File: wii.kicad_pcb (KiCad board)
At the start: 2 copper layers, 60.8 x 24 mm, 12 parts, among them J1 12401598E4#2A, J2 54102-0164, U2 AZ1117-3.3

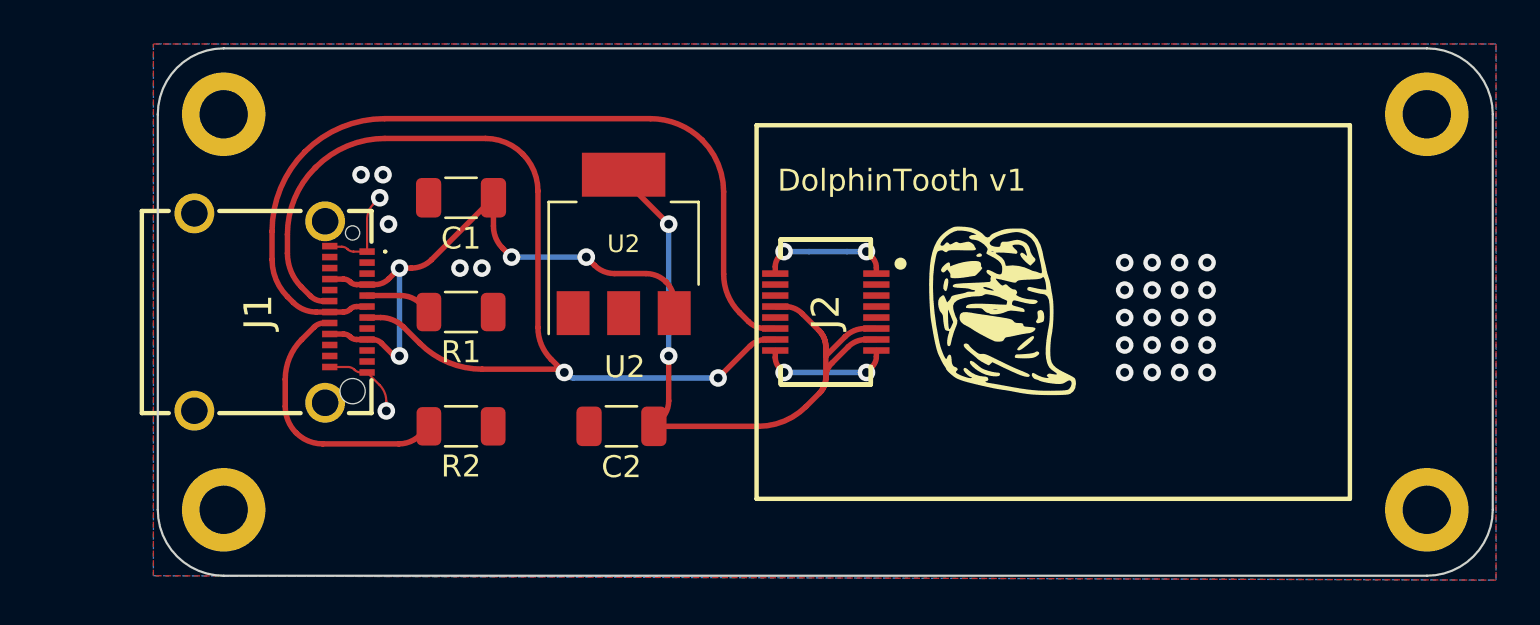
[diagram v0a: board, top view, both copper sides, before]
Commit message: change to usb b
also added html bom plugin and removed round tracks
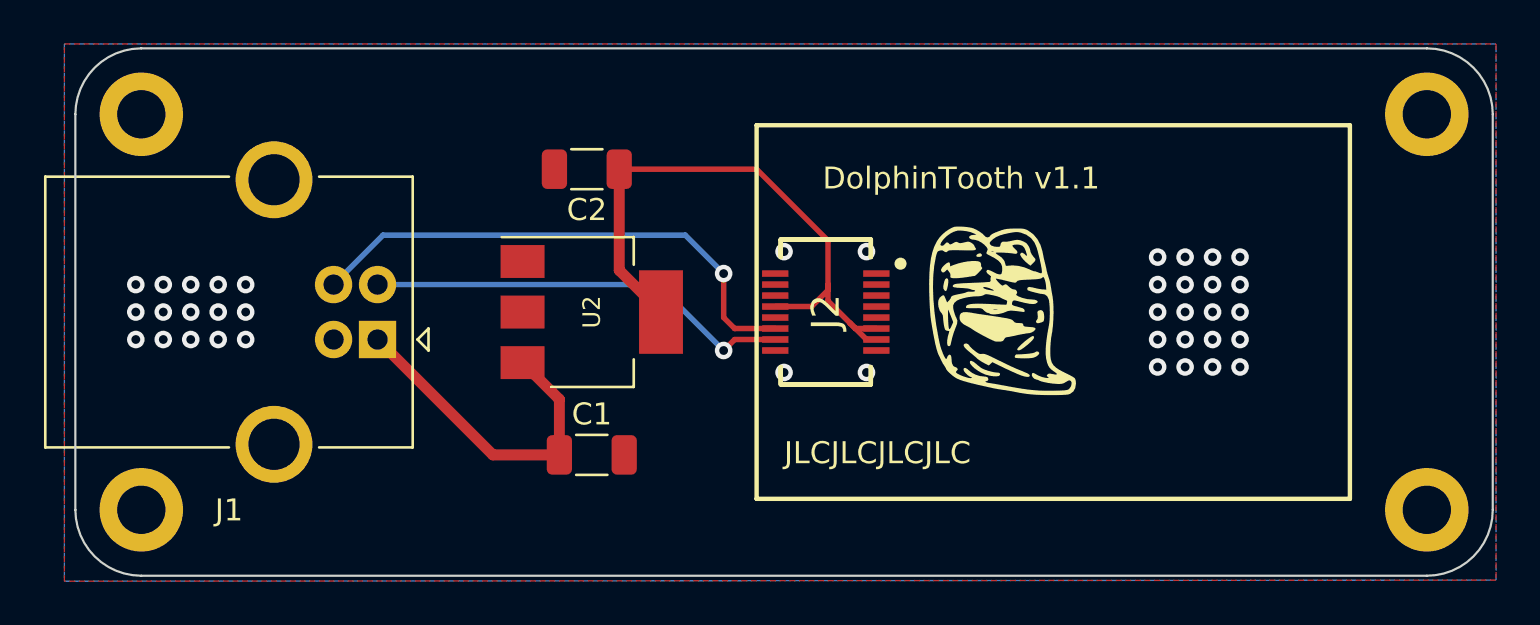
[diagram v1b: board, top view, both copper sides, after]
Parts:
- removed R1, R2: 5.1k, Resistor_SMD:R_1206_3216Metric
- J1: value 12401598E4#2A -> USB_B; footprint SamacSys_Parts:12401598E42A -> Connector_USB:USB_B_OST_USB-B1HSxx_Horizontal
- moved C1 13.1 mm to (128.8, 103.5), turned to 0 degrees
- moved C2 11.8 mm to (128.5, 90.5)
- moved J1 5.64 mm to (119.0, 98.2), turned to 180 degrees
- moved ? 3.75 mm to (108.2, 88.0)
- moved ? 3.75 mm to (108.2, 106.0)
- moved U2 3.42 mm to (128.8, 97.0), turned to 0 degrees
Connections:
- C1 pad 1: Net-(J1-VBUS_1) -> Net-(J1-VBUS)
- J2 pad 10: Net-(J1-D-_1) -> Net-(J1-D-)
- J2 pad 11: Net-(J1-D+_1) -> Net-(J1-D+)
- U2 pad 3: Net-(J1-VBUS_1) -> Net-(J1-VBUS)
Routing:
- net Net-(J1-D-_1): track 48.0 -> 0.00 mm, vias 2 -> 0
- net Net-(J1-D+_1): track 39.9 -> 0.00 mm
- net Net-(J1-VBUS_1): track 28.4 -> 0.00 mm, vias 4 -> 0
- net Net-(J1-D+): track 0.00 -> 24.0 mm, vias 0 -> 1
- net GND: track 20.9 -> 0.00 mm, vias 31 -> 39
- net Net-(J1-D-): track 0.00 -> 19.5 mm, vias 0 -> 1
- net Net-(J1-VBUS): track 0.00 -> 15.3 mm
- net Net-(J1-CC2): track 12.5 -> 0.00 mm
- net Net-(U2-VO): track 34.4 -> 28.1 mm, vias 2 -> 0
- net Net-(J1-CC1): track 3.06 -> 0.00 mm
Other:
- board size 60.8 x 24 mm -> 64.5 x 24 mm
- board text added: "DolphinTooth v1.1"
- board text added: "JLCJLCJLCJLC"
- board text removed: "DolphinTooth v1"
- board text removed: "U2"
